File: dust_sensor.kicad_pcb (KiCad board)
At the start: 2 copper layers, 50 x 32 mm, 26 parts, among them P1 ADC, P2 POWER, P3 LCD, P4 LCD_RST, P5 SERIAL, P6 DHT, P7 SENSOR, P8 GPIOS, SW1 PROG, SW2 RESET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

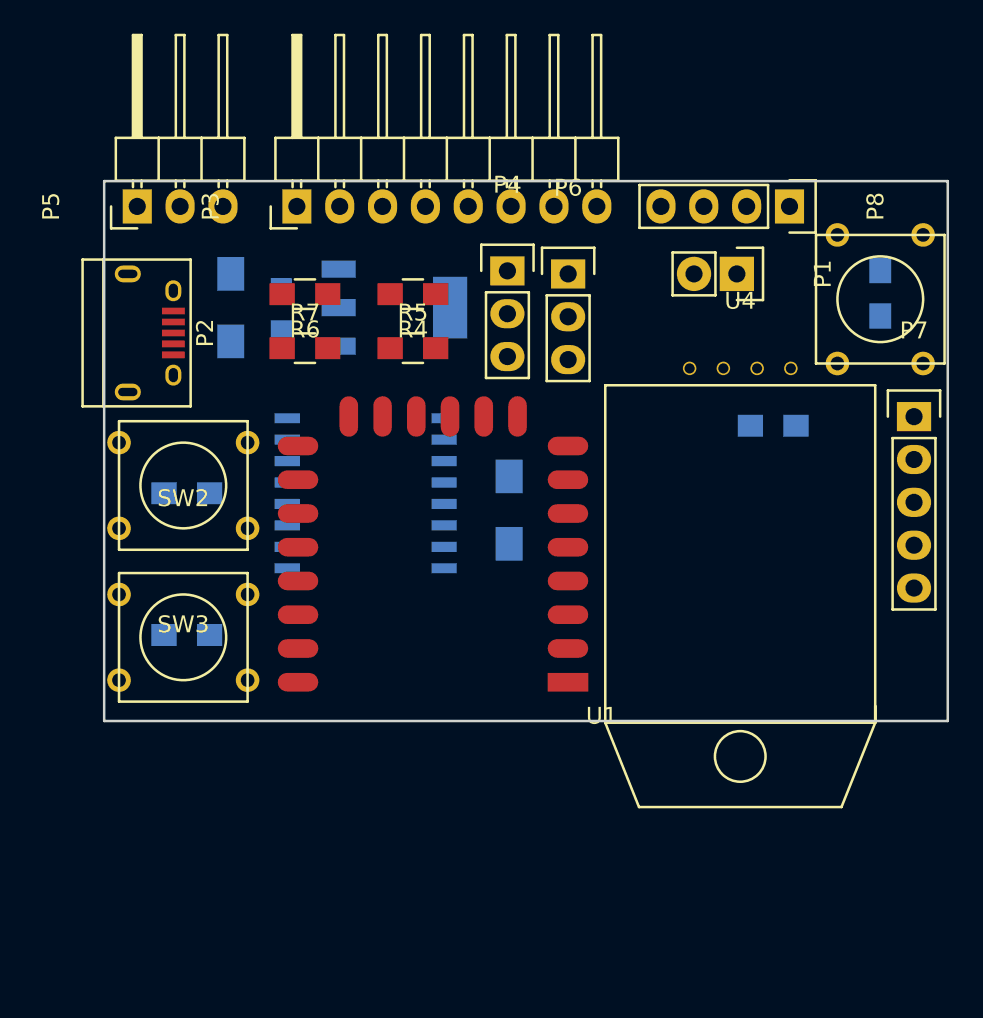
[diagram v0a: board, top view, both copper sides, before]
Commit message: PCB: bigger board + mounting holes
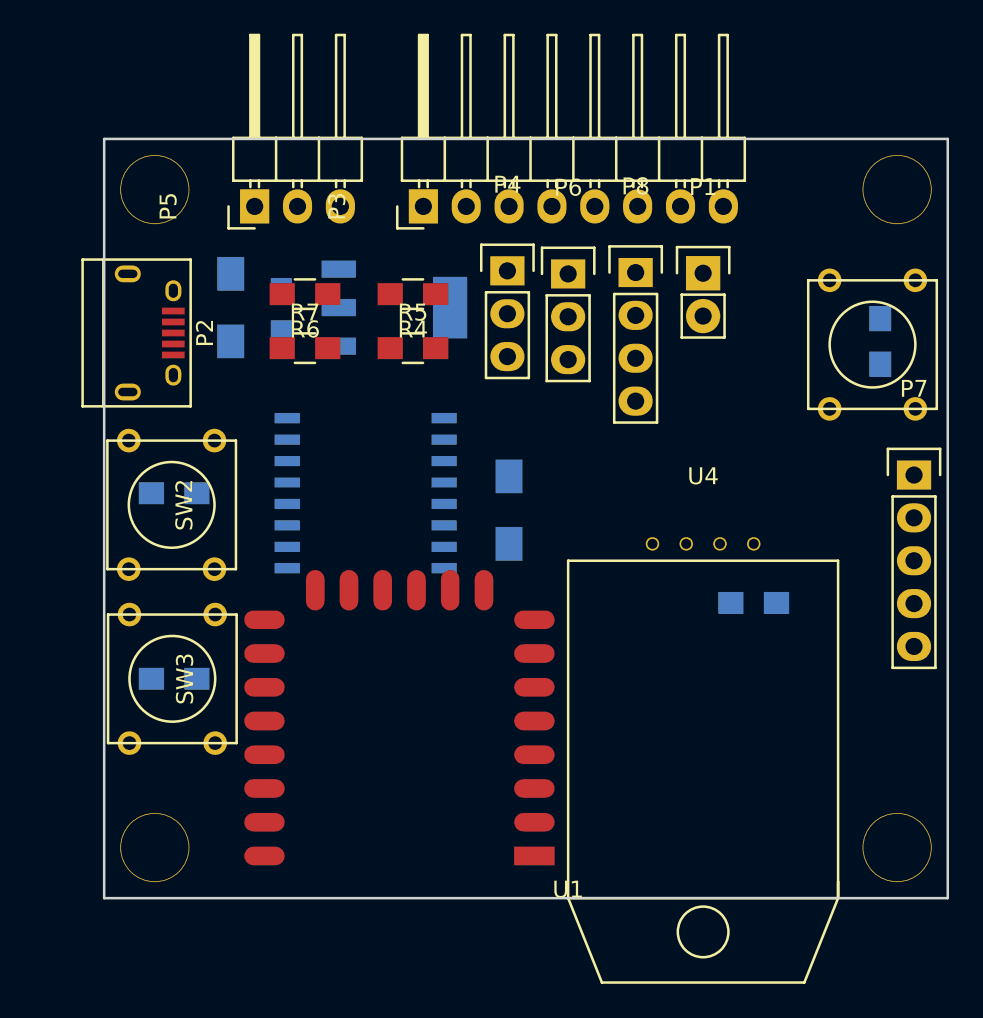
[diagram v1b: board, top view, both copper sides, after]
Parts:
- added ?: , dht:hole_4mm, F.Cu at (86.5, 34.0)
- added ?: , dht:hole_4mm, F.Cu at (42.5, 34.0)
- added ?: , dht:hole_4mm, F.Cu at (42.5, 73.0)
- added ?: , dht:hole_4mm, F.Cu at (86.5, 73.0)
- moved U4 10.6 mm to (75.0, 54.0)
- moved R8 10.6 mm to (78.0, 58.5)
- moved U1 10.5 mm to (65.0, 73.5)
- moved P8 9.93 mm to (71.0, 38.9), turned to 0 degrees
- moved P3 7.50 mm to (58.4, 35.0)
- moved P5 6.96 mm to (48.4, 35.0)
- moved P7 3.46 mm to (87.5, 50.9)
- moved R1 2.85 mm to (85.5, 43.0)
- moved SW1 2.73 mm to (85.0, 43.2)
- moved R3 2.71 mm to (43.6, 63.0)
- moved SW3 2.54 mm to (43.5, 63.0), turned to 270 degrees
- moved P1 2.00 mm to (75.0, 39.0), turned to 0 degrees
- moved SW2 1.34 mm to (43.5, 52.7), turned to 270 degrees
- moved R2 0.75 mm to (43.6, 52.0)
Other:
- board size 50 x 32 mm -> 50 x 45 mm

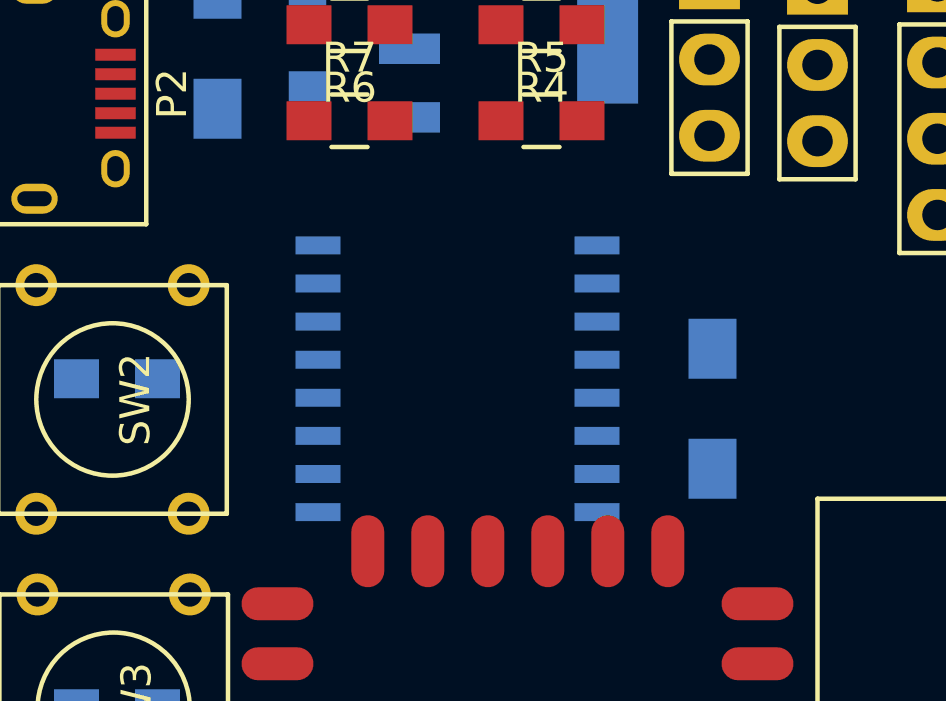
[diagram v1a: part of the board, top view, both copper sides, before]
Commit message: SCH, PCB: add 10uF capacitor at 1117 out
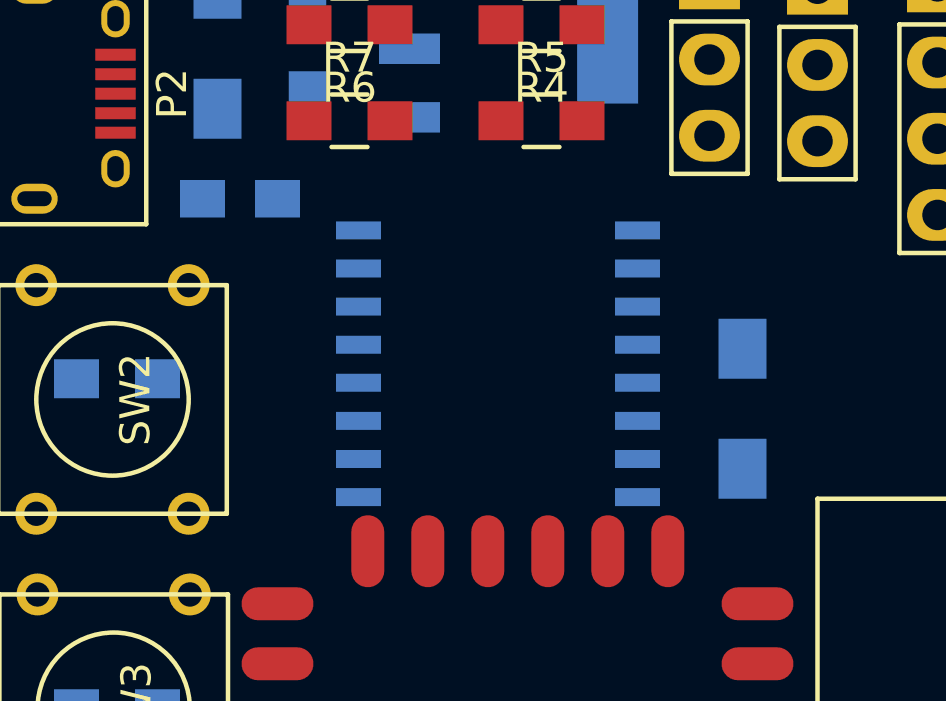
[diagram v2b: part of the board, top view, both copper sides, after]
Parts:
- added C4: 10u, Capacitors_SMD:C_0805_HandSoldering, B.Cu at (47.8, 46.0)
- moved U3 1.44 mm to (56.4, 51.5)
- moved C1 1.00 mm to (64.5, 53.0)
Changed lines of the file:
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@@
 (kicad_pcb (version 4) (host pcbnew no-vcs-found-product)
   (general
-    (links 0)
-    (no_connects 77)
+    (links 79)
+    (no_connects 79)
     (area 39.424999 30.924999 89.575001 76.075001)
     (thickness 1.6)
@@
     (tracks 0)
     (zones 0)
-    (modules 30)
+    (modules 31)
     (nets 29)
   )
@@
   )
   (module Capacitors_SMD:C_1206_HandSoldering (layer B.Cu)
-    (at 63.5 53 90)
+    (at 64.5 53 90)
     (descr "Capacitor SMD 1206, hand soldering")
     (tags "capacitor 1206")
@@
   )
   (module Housings_SOIC:SOIC-16_7.5x10.3mm_Pitch1.27mm (layer B.Cu)
-    (at 55 52 180)
+    (at 56.35 51.5 180)
     (descr "16-Lead Plastic Small Outline (SO) - Wide, 7.50 mm Body [SOIC] (see Microchip Packaging Specification 00000049BS.pdf)")
     (tags "SOIC 1.27")
@@
     (pad 1 thru_hole circle (at 0 0) (size 4.1 4.1) (drill 4) (layers *.Cu *.Mask F.SilkS))
   )
+  (module Capacitors_SMD:C_0805_HandSoldering (layer B.Cu)
+    (at 47.75 46 180)
+    (descr "Capacitor SMD 0805, hand soldering")
+    (tags "capacitor 0805")
+    (attr smd)
+    (fp_text reference C4 (at 0 2.1 180) (layer B.SilkS)
+      (effects (font (size 1 1) (thickness 0.15)) (justify mirror))
+    )
+    (fp_text value 10u (at 0 -2.1 180) (layer B.Fab)
+      (effects (font (size 1 1) (thickness 0.15)) (justify mirror))
+    )
+    (fp_line (start -2.3 1) (end 2.3 1) (layer B.CrtYd) (width 0.05))
+    (fp_line (start -2.3 -1) (end 2.3 -1) (layer B.CrtYd) (width 0.05))
+    (fp_line (start -2.3 1) (end -2.3 -1) (layer B.CrtYd) (width 0.05))
+    (fp_line (start 2.3 1) (end 2.3 -1) (layer B.CrtYd) (width 0.05))
+    (fp_line (start 0.5 0.85) (end -0.5 0.85) (layer B.SilkS) (width 0.15))
+    (fp_line (start -0.5 -0.85) (end 0.5 -0.85) (layer B.SilkS) (width 0.15))
+    (pad 1 smd rect (at -1.25 0 180) (size 1.5 1.25) (layers B.Cu B.Paste B.Mask)
+      (net 1 +3V3))
+    (pad 2 smd rect (at 1.25 0 180) (size 1.5 1.25) (layers B.Cu B.Paste B.Mask)
+      (net 2 GND))
+    (model Capacitors_SMD.3dshapes/C_0805_HandSoldering.wrl
+      (at (xyz 0 0 0))
+      (scale (xyz 1 1 1))
+      (rotate (xyz 0 0 0))
+    )
+  )
   (gr_line (start 39.5 76) (end 39.5 31) (layer Edge.Cuts) (width 0.15))

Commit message: SCH, PCB: add jumper for deep sleep
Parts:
- added P9: DEEP, Pin_Headers:Pin_Header_Straight_1x02, F.Cu at (79.0, 39.0)
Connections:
- U1 pad 4: RESET -> GPIO16
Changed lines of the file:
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@@
 (kicad_pcb (version 4) (host pcbnew no-vcs-found-product)
   (general
-    (links 79)
-    (no_connects 79)
+    (links 80)
+    (no_connects 80)
     (area 39.424999 30.924999 89.575001 76.075001)
     (thickness 1.6)
@@
     (tracks 0)
     (zones 0)
-    (modules 31)
-    (nets 29)
+    (modules 32)
+    (nets 30)
   )
   (page A4)
@@
   (net 27 "Net-(U1-Pad19)")
   (net 28 "Net-(U1-Pad20)")
+  (net 29 GPIO16)
   (net_class Default "This is the default net class."
     (clearance 0.2)
@@
     (add_net DHT_GPIO)
     (add_net GND)
+    (add_net GPIO16)
     (add_net LIGHT)
     (add_net "Net-(P1-Pad1)")
@@
       (net 24 "Net-(R6-Pad1)"))
     (pad 4 smd oval (at 0 6 180) (size 2.4 1.1) (layers F.Cu F.Paste F.Mask)
-      (net 12 RESET))
+      (net 29 GPIO16))
     (pad 5 smd oval (at 0 8 180) (size 2.4 1.1) (layers F.Cu F.Paste F.Mask)
       (net 15 DHT_GPIO))
@@
     )
   )
+  (module Pin_Headers:Pin_Header_Straight_1x02 (layer F.Cu)
+    (at 79 39)
+    (descr "Through hole pin header")
+    (tags "pin header")
+    (fp_text reference P9 (at 0 -5.1) (layer F.SilkS)
+      (effects (font (size 1 1) (thickness 0.15)))
+    )
+    (fp_text value DEEP (at 0 -3.1) (layer F.Fab)
+      (effects (font (size 1 1) (thickness 0.15)))
+    )
+    (fp_line (start 1.27 1.27) (end 1.27 3.81) (layer F.SilkS) (width 0.15))
+    (fp_line (start 1.55 -1.55) (end 1.55 0) (layer F.SilkS) (width 0.15))
+    (fp_line (start -1.75 -1.75) (end -1.75 4.3) (layer F.CrtYd) (width 0.05))
+    (fp_line (start 1.75 -1.75) (end 1.75 4.3) (layer F.CrtYd) (width 0.05))
+    (fp_line (start -1.75 -1.75) (end 1.75 -1.75) (layer F.CrtYd) (width 0.05))
+    (fp_line (start -1.75 4.3) (end 1.75 4.3) (layer F.CrtYd) (width 0.05))
+    (fp_line (start 1.27 1.27) (end -1.27 1.27) (layer F.SilkS) (width 0.15))
+    (fp_line (start -1.55 0) (end -1.55 -1.55) (layer F.SilkS) (width 0.15))
+    (fp_line (start -1.55 -1.55) (end 1.55 -1.55) (layer F.SilkS) (width 0.15))
+    (fp_line (start -1.27 1.27) (end -1.27 3.81) (layer F.SilkS) (width 0.15))
+    (fp_line (start -1.27 3.81) (end 1.27 3.81) (layer F.SilkS) (width 0.15))
+    (pad 1 thru_hole rect (at 0 0) (size 2.032 2.032) (drill 1.016) (layers *.Cu *.Mask F.SilkS)
+      (net 12 RESET))
+    (pad 2 thru_hole oval (at 0 2.54) (size 2.032 2.032) (drill 1.016) (layers *.Cu *.Mask F.SilkS)
+      (net 29 GPIO16))
+    (model Pin_Headers.3dshapes/Pin_Header_Straight_1x02.wrl
+      (at (xyz 0 -0.05 0))
+      (scale (xyz 1 1 1))
+      (rotate (xyz 0 0 90))
+    )
+  )

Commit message: PCB: flip LCD connector
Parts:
- P3: moved to B.Cu
- moved P3 17.6 mm to (76.0, 35.0)

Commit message: PCB, SCH: add current measure jumper
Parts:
- added P10: PWR, Pin_Headers:Pin_Header_Straight_1x02, F.Cu at (79.0, 46.0)
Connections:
- C2 pad 1: +5V -> Net-(C2-Pad1)
- U2 pad 3: +5V -> Net-(C2-Pad1)
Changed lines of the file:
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@@
 (kicad_pcb (version 4) (host pcbnew no-vcs-found-product)
   (general
-    (links 80)
-    (no_connects 80)
+    (links 81)
+    (no_connects 81)
     (area 39.424999 30.924999 89.575001 76.075001)
     (thickness 1.6)
@@
     (tracks 0)
     (zones 0)
-    (modules 32)
-    (nets 30)
+    (modules 33)
+    (nets 31)
   )
   (page A4)
@@
   (net 28 "Net-(U1-Pad20)")
   (net 29 GPIO16)
+  (net 30 "Net-(C2-Pad1)")
   (net_class Default "This is the default net class."
     (clearance 0.2)
@@
     (add_net GPIO16)
     (add_net LIGHT)
+    (add_net "Net-(C2-Pad1)")
     (add_net "Net-(P1-Pad1)")
     (add_net "Net-(P2-Pad6)")
@@
     (fp_line (start -0.5 -0.85) (end 0.5 -0.85) (layer B.SilkS) (width 0.15))
     (pad 1 smd rect (at -1.25 0 90) (size 1.5 1.25) (layers B.Cu B.Paste B.Mask)
-      (net 3 +5V))
+      (net 30 "Net-(C2-Pad1)"))
     (pad 2 smd rect (at 1.25 0 90) (size 1.5 1.25) (layers B.Cu B.Paste B.Mask)
       (net 2 GND))
@@
       (net 1 +3V3))
     (pad 3 smd rect (at 2.286 -3.302 90) (size 1.016 2.032) (layers B.Cu B.Paste B.Mask)
-      (net 3 +5V))
+      (net 30 "Net-(C2-Pad1)"))
     (pad 1 smd rect (at -2.286 -3.302 90) (size 1.016 2.032) (layers B.Cu B.Paste B.Mask)
       (net 2 GND))
@@
     (model Pin_Headers.3dshapes/Pin_Header_Straight_1x02.wrl
       (at (xyz 0 -0.05 0))
+      (scale (xyz 1 1 1))
+      (rotate (xyz 0 0 90))
+    )
+  )
+  (module Pin_Headers:Pin_Header_Straight_1x02 (layer F.Cu)
+    (at 79 46)
+    (descr "Through hole pin header")
+    (tags "pin header")
+    (fp_text reference P10 (at 0 -5.1) (layer F.SilkS)
+      (effects (font (size 1 1) (thickness 0.15)))
+    )
+    (fp_text value PWR (at 0 -3.1) (layer F.Fab)
+      (effects (font (size 1 1) (thickness 0.15)))
+    )
+    (fp_line (start 1.27 1.27) (end 1.27 3.81) (layer F.SilkS) (width 0.15))
+    (fp_line (start 1.55 -1.55) (end 1.55 0) (layer F.SilkS) (width 0.15))
+    (fp_line (start -1.75 -1.75) (end -1.75 4.3) (layer F.CrtYd) (width 0.05))
+    (fp_line (start 1.75 -1.75) (end 1.75 4.3) (layer F.CrtYd) (width 0.05))
+    (fp_line (start -1.75 -1.75) (end 1.75 -1.75) (layer F.CrtYd) (width 0.05))
+    (fp_line (start -1.75 4.3) (end 1.75 4.3) (layer F.CrtYd) (width 0.05))
+    (fp_line (start 1.27 1.27) (end -1.27 1.27) (layer F.SilkS) (width 0.15))
+    (fp_line (start -1.55 0) (end -1.55 -1.55) (layer F.SilkS) (width 0.15))
+    (fp_line (start -1.55 -1.55) (end 1.55 -1.55) (layer F.SilkS) (width 0.15))
+    (fp_line (start -1.27 1.27) (end -1.27 3.81) (layer F.SilkS) (width 0.15))
+    (fp_line (start -1.27 3.81) (end 1.27 3.81) (layer F.SilkS) (width 0.15))
+    (pad 1 thru_hole rect (at 0 0) (size 2.032 2.032) (drill 1.016) (layers *.Cu *.Mask F.SilkS)
+      (net 30 "Net-(C2-Pad1)"))
+    (pad 2 thru_hole oval (at 0 2.54) (size 2.032 2.032) (drill 1.016) (layers *.Cu *.Mask F.SilkS)
+      (net 3 +5V))
+    (model Pin_Headers.3dshapes/Pin_Header_Straight_1x02.wrl
+      (at (xyz 0 -0.05 0))
